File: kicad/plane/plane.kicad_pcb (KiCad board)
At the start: 2 copper layers, 23 parts, among them M1 Left_Aileron_Servo, M2 Right_Aileron_Servo, M3 Elevator_Servo, M4 Rudder_Servo, U1 LD1085V50, U10 ADS1115, U11 GY - GPS6MV2, U3 LD1085V50, U4 ESP32_DevKit_1, U5 AMS1117-3.3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

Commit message: pcb components placement
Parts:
- added J1: Battery, PlaneFootprints:14AWG_Wire, F.Cu at (139.0, 72.0)
- added U2: ESC, PlaneFootprints:ESC, F.Cu at (158.0, 78.5)
- moved D1 220.0 mm to (257.6, 90.5), turned to -90 degrees
- moved D2 211.4 mm to (250.5, 90.5), turned to -90 degrees
- moved D3 202.9 mm to (243.4, 90.5), turned to -90 degrees
- moved D4 194.6 mm to (236.3, 90.5), turned to -90 degrees
- moved U11 187.6 mm to (290.7, 98.3), turned to 90 degrees
- moved U8 172.1 mm to (253.0, 108.0), turned to -90 degrees
- moved U3 120.7 mm to (161.0, 100.3), turned to -90 degrees
- moved U1 115.7 mm to (149.0, 100.3), turned to -90 degrees
- moved M3 106.1 mm to (154.9, 112.5), turned to 180 degrees
- moved M2 105.8 mm to (150.0, 112.5), turned to 180 degrees
- moved M4 105.8 mm to (159.2, 112.5), turned to 180 degrees
- moved M1 105.8 mm to (145.4, 112.5), turned to 180 degrees
- moved U10 83.4 mm to (103.5, 81.9), turned to 180 degrees
- moved R4 80.1 mm to (204.5, 77.3), turned to 90 degrees
- moved R3 78.5 mm to (200.4, 77.3), turned to 90 degrees
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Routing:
- net Net-(M1-+): track 0.00 -> 1.06 mm
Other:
- board outline added: 172 x 50 mm

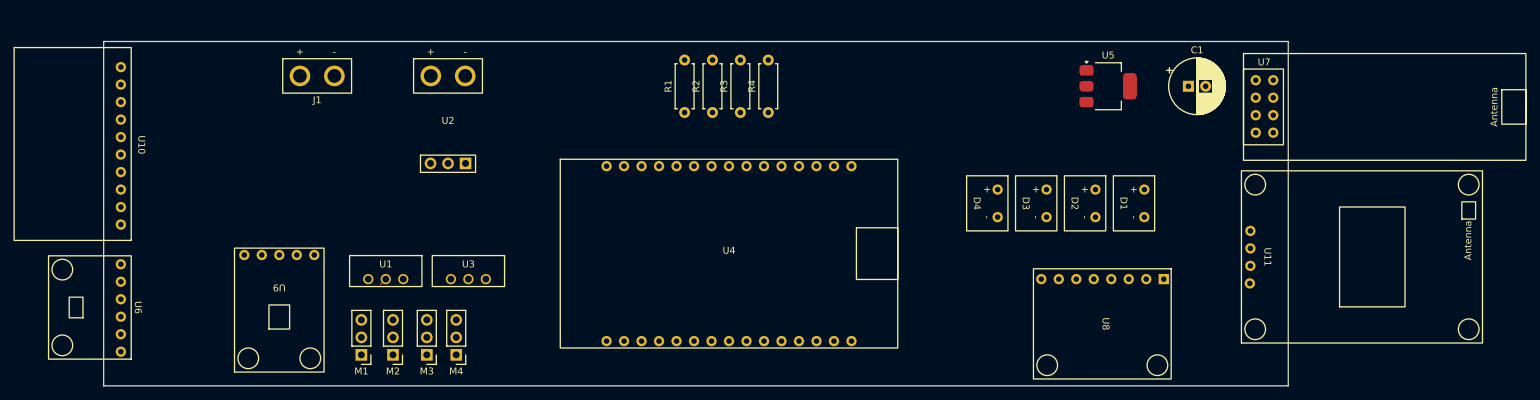
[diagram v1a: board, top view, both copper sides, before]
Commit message: pcb without sensors (just rc) is ready to production hehehe
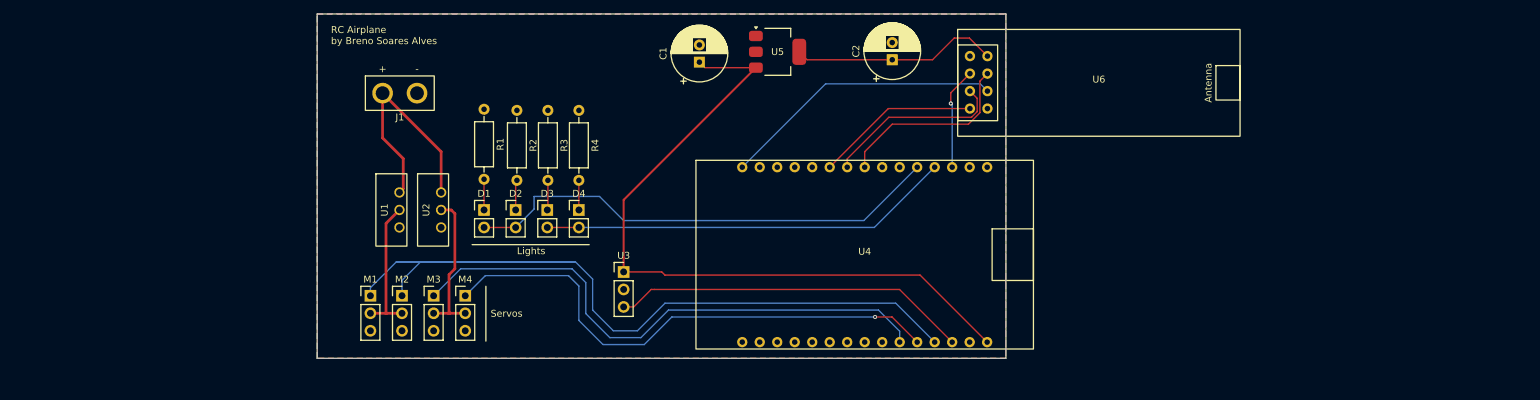
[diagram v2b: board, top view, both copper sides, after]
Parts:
- removed U10: ADS1115, PlaneFootprints:ADS1115
- removed U11: GY - GPS6MV2, PlaneFootprints:GPS6MV2
- removed U7: nRF24L01+, PlaneFootprints:nRF24L01+
- removed U8: GY-521 - MPU6050, PlaneFootprints:MPU6050
- removed U9: GY273 - HMC5883L, PlaneFootprints:HMC5883L
- added C2: 10uF, Capacitor_THT:CP_Radial_D8.0mm_P2.50mm, F.Cu at (222.5, 69.7)
- C1: value 10uF -> 100uF
- D1, D2, D3, D4: footprint PlaneFootprints:LED -> Connector_PinHeader_2.54mm:PinHeader_1x02_P2.54mm_Vertical
- M1: value Left_Aileron_Servo -> Left_Aileron
- M2: value Right_Aileron_Servo -> Right_Aileron
- M3: value Elevator_Servo -> Elevator
- M4: value Rudder_Servo -> Rudder
- R1, R2, R3, R4: footprint Resistor_THT:R_Axial_DIN0207_L6.3mm_D2.5mm_P7.62mm_Horizontal -> Resistor_THT:R_Axial_DIN0207_L6.3mm_D2.5mm_P10.16mm_Horizontal
- U2: value ESC -> LD1085V50; footprint PlaneFootprints:ESC -> PlaneFootprints:LD1085V50
- U3: value LD1085V50 -> ESC; footprint PlaneFootprints:LD1085V50 -> Connector_PinHeader_2.54mm:PinHeader_1x03_P2.54mm_Vertical
- U6: value GY - BMP280 -> nRF24L01+; footprint PlaneFootprints:BMP280 -> PlaneFootprints:nRF24L01+
- moved U6 150.1 mm to (252.5, 73.0), turned to 0 degrees
- moved D1 94.4 mm to (163.2, 91.5), turned to 0 degrees
- moved D2 82.7 mm to (167.8, 91.5), turned to 0 degrees
- moved C1 71.1 mm to (194.5, 70.0), turned to 90 degrees
- moved D3 71.0 mm to (172.4, 91.5), turned to 0 degrees
- moved D4 59.3 mm to (177.0, 91.5), turned to 0 degrees
- moved U5 48.3 mm to (205.8, 68.5)
- moved R1 29.1 mm to (163.2, 76.8), turned to -90 degrees
- moved R2 28.4 mm to (168.0, 77.0), turned to -90 degrees
- moved R3 28.0 mm to (172.5, 77.0), turned to -90 degrees
- moved R4 27.5 mm to (177.0, 77.0), turned to -90 degrees
- moved U3 22.5 mm to (183.5, 100.5), turned to 0 degrees
- moved U4 19.7 mm to (218.5, 98.0)
- moved U2 13.1 mm to (155.8, 91.5)
- moved J1 12.3 mm to (151.0, 74.5)
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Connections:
- C1 pad 1: Net-(U5-VO) -> Net-(U3-5V)
- U2 pad 2: GND -> Net-(M3-+)
- U2 pad 3: Net-(U10-VDD) -> GND
- U3 pad 1: Net-(J1-Pin_2) -> Net-(U3-5V)
- U3 pad 2: Net-(M3-+) -> GND
- U3 pad 3: GND -> Net-(U3-PWM)
- U4 pad 10: Net-(U11-TX) -> unconnected-(U4-RX2-Pad10)
- U4 pad 11: Net-(U4-D4) -> Net-(D1-A)
- U4 pad 12: unconnected-(U4-D2-Pad12) -> Net-(D3-A)
- U4 pad 13: unconnected-(U4-D15-Pad13) -> Net-(U4-D15)
- U4 pad 14: Net-(U11-GND) -> unconnected-(U4-GND-Pad14)
- U4 pad 15: Net-(U11-VCC) -> unconnected-(U4-3V3-Pad15)
- U4 pad 2: Net-(U10-SCL) -> unconnected-(U4-D22-Pad2)
- U4 pad 23: Net-(D3-A) -> unconnected-(U4-D25-Pad23)
- U4 pad 24: Net-(D1-A) -> unconnected-(U4-D26-Pad24)
- U4 pad 25: Net-(U2-PWM) -> Net-(M3-PWM)
- U4 pad 26: Net-(M1-PWM) -> Net-(M4-PWM)
- U4 pad 27: Net-(M3-PWM) -> Net-(M1-PWM)
- U4 pad 28: Net-(M4-PWM) -> Net-(U3-PWM)
- U4 pad 30: Net-(U10-VDD) -> Net-(U3-5V)
- U4 pad 5: Net-(U10-SDA) -> unconnected-(U4-D21-Pad5)
- U4 pad 9: Net-(U11-RX) -> unconnected-(U4-TX2-Pad9)
- U5 pad 3: Net-(U10-VDD) -> Net-(U3-5V)
- U6 pad 1: Net-(U11-VCC) -> Net-(U5-VO)
- U6 pad 2: Net-(U11-GND) -> GND
- U6 pad 3: Net-(U10-SCL) -> Net-(U4-D15)
- U6 pad 4: Net-(U10-SDA) -> Net-(U4-D5)
- U6 pad 5: Net-(U11-VCC) -> Net-(U4-D18)
- U6 pad 6: Net-(U11-GND) -> Net-(U4-D23)
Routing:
- net Net-(M1-PWM): track 0.00 -> 127.4 mm
- net Net-(U3-5V): track 0.00 -> 103.1 mm
- net Net-(M3-PWM): track 0.00 -> 80.6 mm
- net Net-(M4-PWM): track 0.00 -> 77.1 mm, vias 0 -> 1
- net Net-(D1-A): track 0.00 -> 70.5 mm
- net Net-(D3-A): track 0.00 -> 59.9 mm
- net Net-(U3-PWM): track 0.00 -> 51.9 mm
- net Net-(U4-D23): track 0.00 -> 41.0 mm
- net Net-(J1-Pin_2): track 0.00 -> 33.8 mm
- net Net-(U5-VO): track 0.00 -> 30.2 mm
- net Net-(U4-D5): track 0.00 -> 27.5 mm
- net Net-(U4-D18): track 0.00 -> 26.3 mm
- net Net-(U4-D19): track 0.00 -> 23.9 mm
- net Net-(M3-+): track 0.00 -> 21.6 mm
- net Net-(M1-+): track 1.06 -> 20.5 mm
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- added copper zone on B.Cu, net GND
- added copper zone on F.Cu, net GND
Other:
- board size 172 x 50 mm -> 100 x 50 mm
- board text added: "Lights"
- board text added: "RC Airplane by Breno Soares Alves"
- board text added: "Servos"

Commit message: defined 16awg wire for battery connection and first pcb finished
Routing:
- net Net-(U5-VO): track 30.2 -> 36.5 mm
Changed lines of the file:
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@@
 			)
 		)
-		(property "Description" "Generic connector, single row, 01x02, script generated (kicad-library-utils/schlib/autogen/connector/)"
+		(property "Description" ""
 			(at 0 0 0)
 			(unlocked yes)
@@
 			(at 2.5 0)
 			(size 3 3)
-			(drill 2)
+			(drill 1.6)
 			(layers "*.Cu" "*.Mask")
 			(remove_unused_layers no)
@@
 			(at -2.5 0)
 			(size 3 3)
-			(drill 2)
+			(drill 1.6)
 			(layers "*.Cu" "*.Mask")
 			(remove_unused_layers no)
@@
 		(width 0.2)
 		(layer "F.Cu")
+		(net 3)
+	)
+	(segment
+		(start 202.7 68.5)
+		(end 209 68.5)
+		(width 0.2)
+		(layer "F.Cu")
